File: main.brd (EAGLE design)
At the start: 24.4 x 26.2 mm, 45 parts, among them IC1 ATTINY13A-SSH, IC2 TP4056-42-ESOP8, IC3 LM27313XMFX_NOPB, IC4 TPL5110DDCT, IC5 ATTINY13A-SSH, T1A 2N4401, T1B NPN, X1 MINI-USB-UX60A-MB-5ST, X2 332-02

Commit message: updates
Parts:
- moved C2 0.61 mm to (4.27, 3.05)
- turned R5 to 270 degrees
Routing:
- net SENSOR+: track 17.9 -> 16.2 mm
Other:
- board text added: "(C) 2020 tinyplant.ca"
- board text removed: "(C) 2020 Dima Dykhman"

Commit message: updates
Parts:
- added R15: 0R, resistor:R0402
- moved R14 5.94 mm to (15.8, 8.99), flipped to the top
- moved R12 5.66 mm to (5.94, 7.92), turned to 180 degrees
- moved R5 2.13 mm to (13.1, 7.92)
- moved C2 1.41 mm to (3.35, 4.11), turned to 270 degrees
- moved C1 0.91 mm to (20.9, 9.91), turned to 270 degrees
- moved D2 0.89 mm to (6.25, 5.18)
- moved D1 0.55 mm to (20.9, 5.49)
- moved R6 0.46 mm to (10.5, 7.92)
- moved REG1A 0.43 mm to (3.35, 9.91)
- moved IC1 0.34 mm to (13.4, 13.9)
- moved R11 0.30 mm to (21.6, 10.8)
- moved R13 0.30 mm to (21.6, 8.84)
- moved T1A 0.30 mm to (22.7, 18.3)
- moved C4 0.15 mm to (13.6, 22.9)
- moved IC4 0.15 mm to (17.2, 3.81)
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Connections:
- new net N$16: IC5.5, R15.1
- net SOLAR_REG+/-: now also R15.2; no longer IC5.5
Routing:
- net N$16: track 0.00 -> 10.1 mm, vias 0 -> 1
- net SOLAR_REG+/-: track 34.7 -> 25.3 mm, vias 1 -> 0
- net NPN+: track 16.2 -> 22.8 mm
- net GND: track 53.3 -> 59.4 mm
- net N$5: track 75.6 -> 71.1 mm
- net N$14: track 15.6 -> 11.4 mm
- net SOLAR_PANEL+: track 15.3 -> 12.5 mm
- net N$13: track 19.7 -> 16.9 mm
- net SENSOR-: track 9.38 -> 7.60 mm
- net N$3: track 21.1 -> 22.9 mm
- net SENSOR+: track 16.2 -> 14.6 mm
- net RESET: track 13.8 -> 12.2 mm
- net VCC: track 11.7 -> 10.6 mm
- net N$4: track 58.6 -> 57.6 mm
- net N$15: track 4.91 -> 5.69 mm, vias 0 -> 1
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
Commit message: updates
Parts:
- R14: value 0R -> 10k
- moved R12 3.77 mm to (3.35, 5.18), turned to 90 degrees
- moved C2 2.29 mm to (4.72, 2.29), turned to 0 degrees
- moved REG1A 0.34 mm to (3.66, 9.75)
- moved PUMP- 0.15 mm to (22.6, 13.7)
- moved D2 0.15 mm to (6.25, 5.33)
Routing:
- net SOLAR_PANEL+: track 12.5 -> 16.5 mm
- net N$12: track 7.04 -> 10.6 mm
- net GND: track 59.4 -> 56.6 mm
- net N$14: track 11.4 -> 12.5 mm
- net N$5: track 71.1 -> 71.9 mm

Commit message: lots of updates
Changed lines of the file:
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@@
 <wire x1="17.8562" y1="14.5034" x2="15.8242" y2="14.5034" width="0.1524" layer="1"/>
 <contactref element="R7" pad="1"/>
-<wire x1="19.05" y1="15.0876" x2="18.4404" y2="15.0876" width="0.1524" layer="16"/>
-<wire x1="18.4404" y1="15.0876" x2="18.288" y2="14.9352" width="0.1524" layer="16"/>
+<wire x1="19.2024" y1="14.9352" x2="18.288" y2="14.9352" width="0.1524" layer="16"/>
 <wire x1="21.7932" y1="18.7452" x2="20.8788" y2="19.6596" width="0.1524" layer="16"/>
 <wire x1="20.8788" y1="19.9644" x2="20.8788" y2="19.6596" width="0.1524" layer="16"/>
@@
 <wire x1="19.2278" y1="11.2522" x2="19.812" y2="11.8364" width="0.1524" layer="16"/>
 <wire x1="19.812" y1="11.8364" x2="19.812" y2="14.3256" width="0.1524" layer="16"/>
-<wire x1="19.812" y1="14.3256" x2="19.05" y2="15.0876" width="0.1524" layer="16"/>
+<wire x1="19.812" y1="14.3256" x2="19.2024" y2="14.9352" width="0.1524" layer="16"/>
 <wire x1="21.7932" y1="17.8308" x2="21.0312" y2="17.0688" width="0.1524" layer="16"/>
 <wire x1="21.0312" y1="17.0688" x2="20.4216" y2="17.0688" width="0.1524" layer="16"/>

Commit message: rev 0.9
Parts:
- removed PAD1: (no value), wirepad:1,6/0,8
- added R16: 100R, resistor:R0603
- C4: device rcl:C1206 -> rcl:C0805
- D1, D2: value BZX84CSMD -> (none); device diode:TO236 -> led:SML0805
- R1: value 1k -> 100R
- R10: device resistor:R0805 -> resistor:R0603
- R13: value 1.5k -> 2.2k
- R7: device resistor:R0603 -> resistor:R0805
- T1B: device semicon-smd-ipc:SOT23W -> zetex:SOT-23
- moved R12 8.73 mm to (11.0, 9.45), turned to 0 degrees
- moved R9 6.71 mm to (8.23, 20.3), turned to 90 degrees
- moved R7 4.64 mm to (14.2, 19.8), turned to 90 degrees
- moved T1B 3.51 mm to (17.4, 19.8), turned to 90 degrees
- moved R8 2.76 mm to (18.3, 20.3), turned to 270 degrees
- moved X2 2.14 mm to (19.7, 22.9), turned to 270 degrees
- moved R1 1.70 mm to (10.5, 19.8), turned to 270 degrees
- moved IC5 1.22 mm to (13.4, 13.0)
- moved C1 0.78 mm to (21.6, 10.1), turned to 180 degrees
- moved LED1 0.63 mm to (12.9, 22.8)
- moved T1A 0.48 mm to (22.6, 18.7)
- moved IC2 0.46 mm to (13.4, 19.5)
- moved X1 0.46 mm to (13.3, 4.72)
- moved D2 0.34 mm to (6.10, 5.64), turned to 270 degrees
- moved R13 0.34 mm to (21.3, 8.69)
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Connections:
- new net N$17: IC5.8, R16.1
- net GND: now also T1B.2; no longer T1B.3
- net N$1: now also T1B.3; no longer T1B.1
- net N$2: now also T1B.1; no longer T1B.2
- net N$5: now also R16.2; no longer IC5.8
- net N$6: no longer PAD1.1
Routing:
- net GND: track 56.6 -> 9.33 mm
- net VCC: track 10.6 -> 36.7 mm, vias 1 -> 0
- net N$5: track 71.9 -> 61.4 mm
- net LED: track 22.4 -> 12.5 mm, vias 1 -> 0
- net N$4: track 57.6 -> 48.9 mm
- net N$6: track 9.18 -> 2.27 mm
- net N$12: track 10.6 -> 4.27 mm
- net N$13: track 17.1 -> 22.9 mm
- net N$2: track 14.9 -> 9.34 mm
- net N$8: track 7.29 -> 2.39 mm
- net N$1: track 19.0 -> 23.0 mm
- net N$17: track 0.00 -> 2.80 mm
- net NPN+: track 22.8 -> 20.4 mm
- net N$3: track 22.9 -> 21.0 mm
- net N$14: track 12.5 -> 11.0 mm
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- added copper zone on layer 16, net GND
- removed copper zone on layer 16, net VCC
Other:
- board text added: "Rev 0.9"
- board text removed: "Rev 0.8"

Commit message: updates
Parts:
- removed X2: 332-02, con-garry:332-02
- added JP1: (no value), pinhead:1X02/90
- added R17: 100R, resistor:R0603
- moved R8 1.10 mm to (19.2, 19.7), turned to 0 degrees
- moved T1A 0.82 mm to (22.9, 18.0)
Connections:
- new net N$18: IC3.4, R17.2, REG1A.2
- net SOLAR_REG+/-: now also R17.1; no longer IC3.4, REG1A.2
- net VCC: now also JP1.2; no longer X2.1
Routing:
- net N$18: track 0.00 -> 8.36 mm
- net SOLAR_REG+/-: track 24.0 -> 18.9 mm
- net N$9: track 21.7 -> 17.0 mm
- net GND: track 9.33 -> 5.72 mm, vias 0 -> 1
- net SOLAR_PANEL+: track 15.3 -> 16.9 mm
- net VCC: track 36.7 -> 38.2 mm
- net N$1: track 23.0 -> 23.7 mm

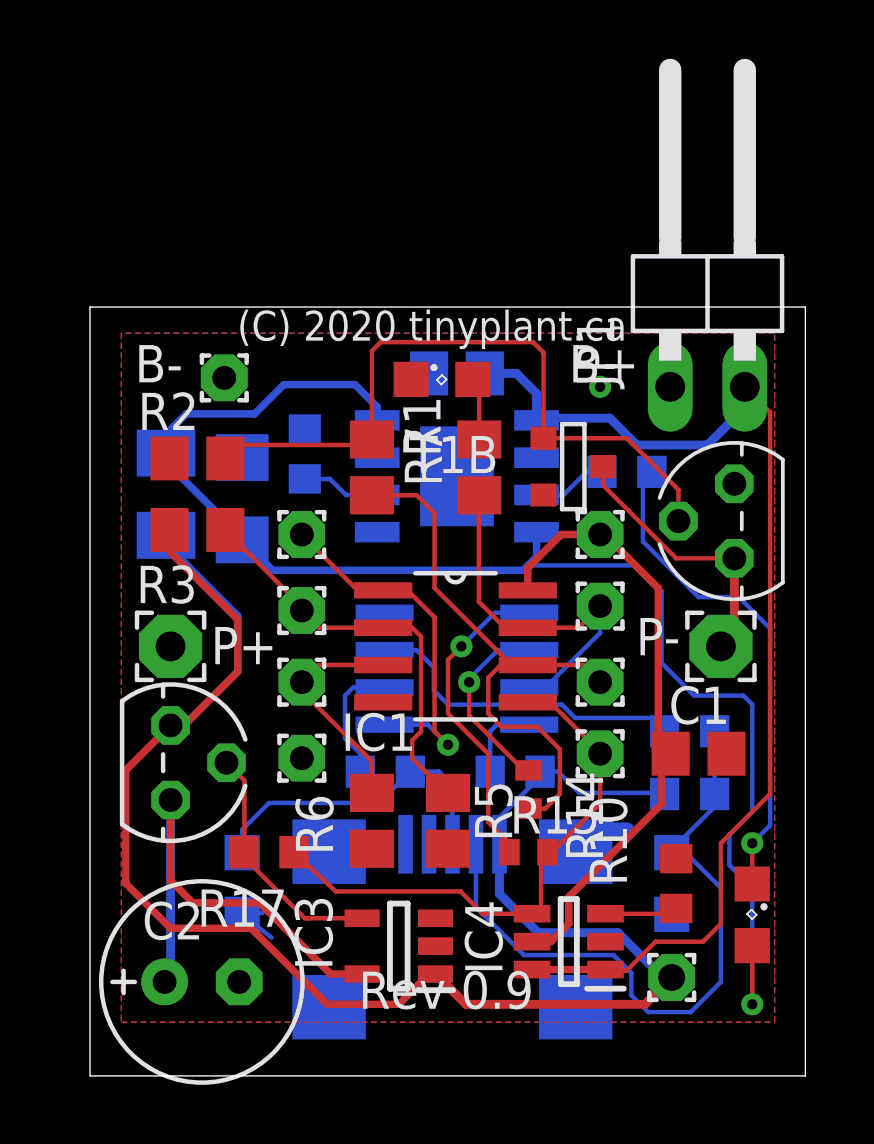
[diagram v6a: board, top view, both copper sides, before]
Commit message: added usb diode
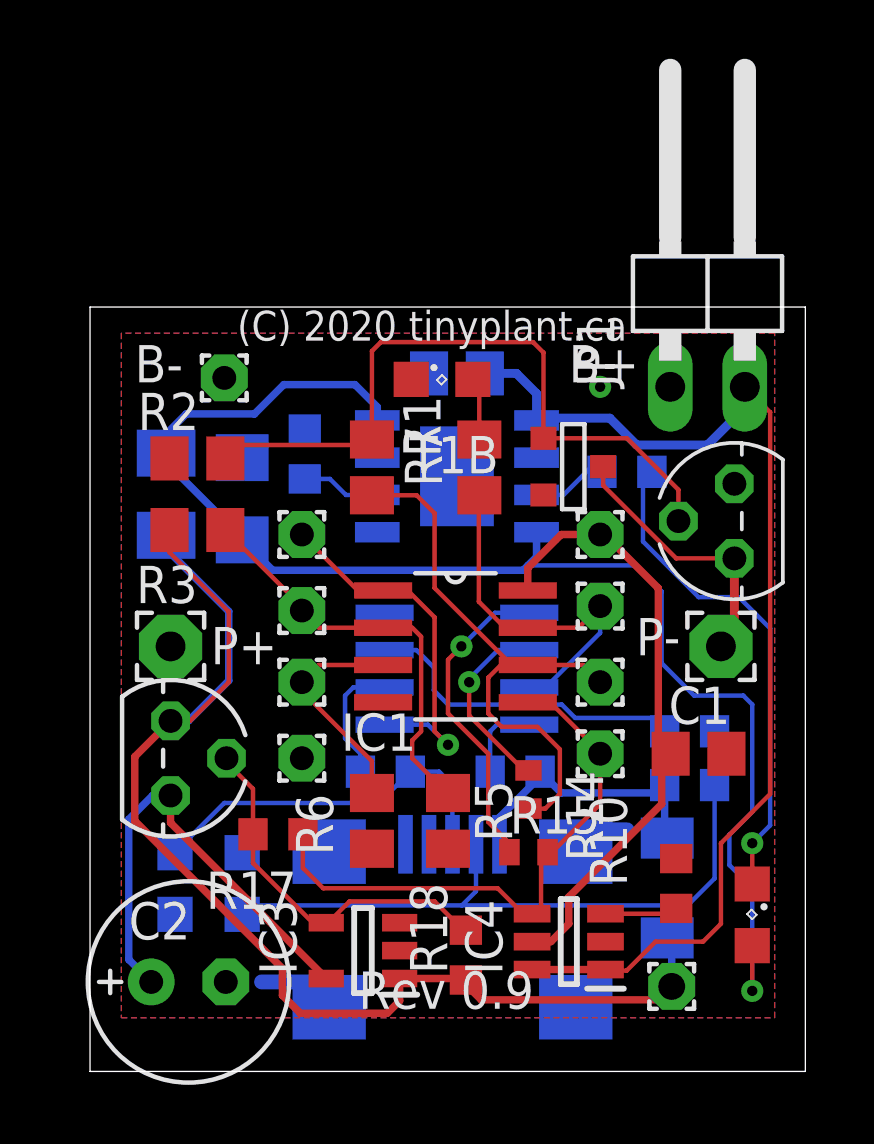
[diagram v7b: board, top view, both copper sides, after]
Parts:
- added D3: (no value), diode:MINIMELF
- added R18: 400R, resistor:R0603
- R4: value R400 -> 0R
- moved D1 14.6 mm to (6.10, 5.64), turned to 90 degrees
- moved D2 2.29 mm to (3.81, 5.64)
- moved IC3 1.23 mm to (10.2, 3.35)
- moved R17 0.68 mm to (7.32, 7.32)
- moved C2 0.46 mm to (4.27, 2.29)
- moved IN+ 0.30 mm to (20.7, 2.13)
- moved R13 0.30 mm to (21.3, 8.99)
- moved REG1A 0.15 mm to (3.66, 9.91)
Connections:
- new net N$21: D3.A, R13.1, R16.2, X1.1
- net N$18: now also R18.2
- net N$5: now also D3.C, R18.1; no longer R13.1, R16.2, X1.1
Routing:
- net N$5: track 61.4 -> 45.6 mm
- net N$21: track 0.00 -> 9.54 mm
- net N$18: track 8.36 -> 12.7 mm
- net N$14: track 11.0 -> 12.8 mm
- net N$13: track 22.9 -> 23.9 mm
- net N$4: track 48.7 -> 47.8 mm
- net SOLAR_PANEL+: track 16.9 -> 16.0 mm
- net SOLAR_REG+/-: track 18.9 -> 19.5 mm
- net GND: track 5.72 -> 6.28 mm
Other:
- board size 24.4 x 26.2 mm -> 24.4 x 26 mm

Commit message: low battery detection
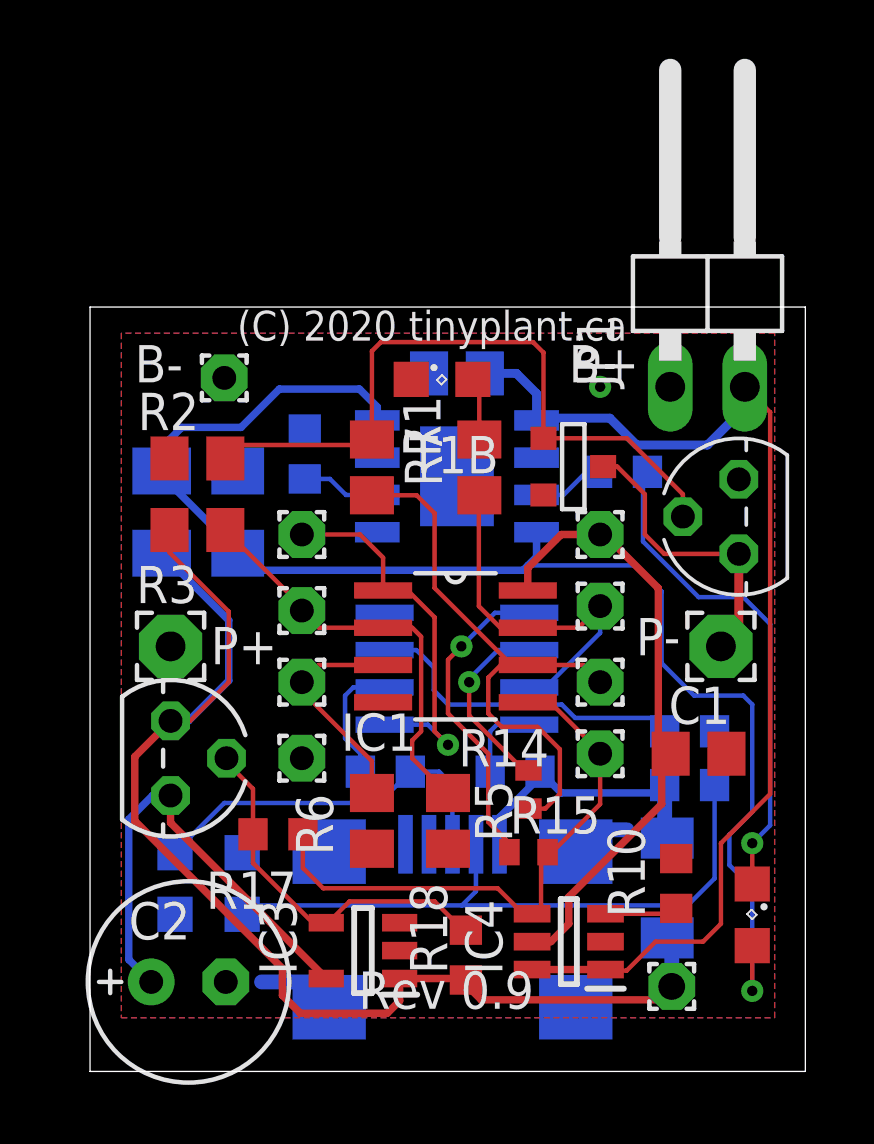
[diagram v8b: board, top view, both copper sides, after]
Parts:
- moved R4 0.63 mm to (3.35, 18.3)
- moved C3 0.48 mm to (5.94, 18.3)
- moved T1A 0.22 mm to (23.0, 18.1)
- moved R8 0.15 mm to (19.1, 19.7)
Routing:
- net N$2: track 9.32 -> 10.1 mm
- net RESET: track 12.7 -> 13.3 mm
- net N$5: track 45.6 -> 45.1 mm
